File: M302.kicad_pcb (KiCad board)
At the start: 2 copper layers, 68.6 x 53.3 mm, 23 parts, among them J1 I2C-1, J2 I2C-2, J3 I2C-3, J4 I2C-4, J5 I2C-D400, J6 W5500, J7 IM920, J8 PWR, J9 VSW, P1 Power, P2 Analog, P3 Digital, P4 Digital, P5 CONN_01X01, P6 CONN_01X01, P7 CONN_01X01, P8 CONN_01X01, SW1 CPU_RESET, SW2 D400_RESET, SW3 IM920_RESET, U1 SFE-BOB-12009

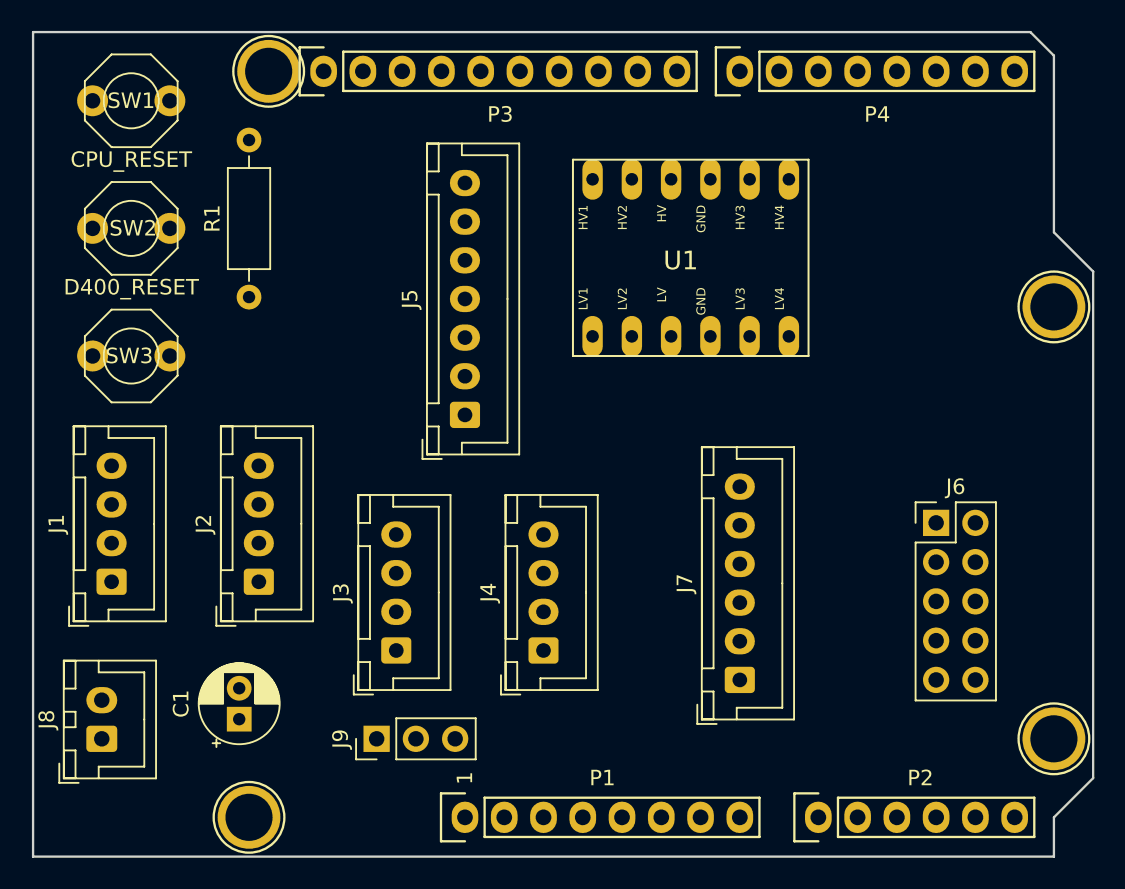
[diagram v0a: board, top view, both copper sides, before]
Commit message: VSWは不要なので外す
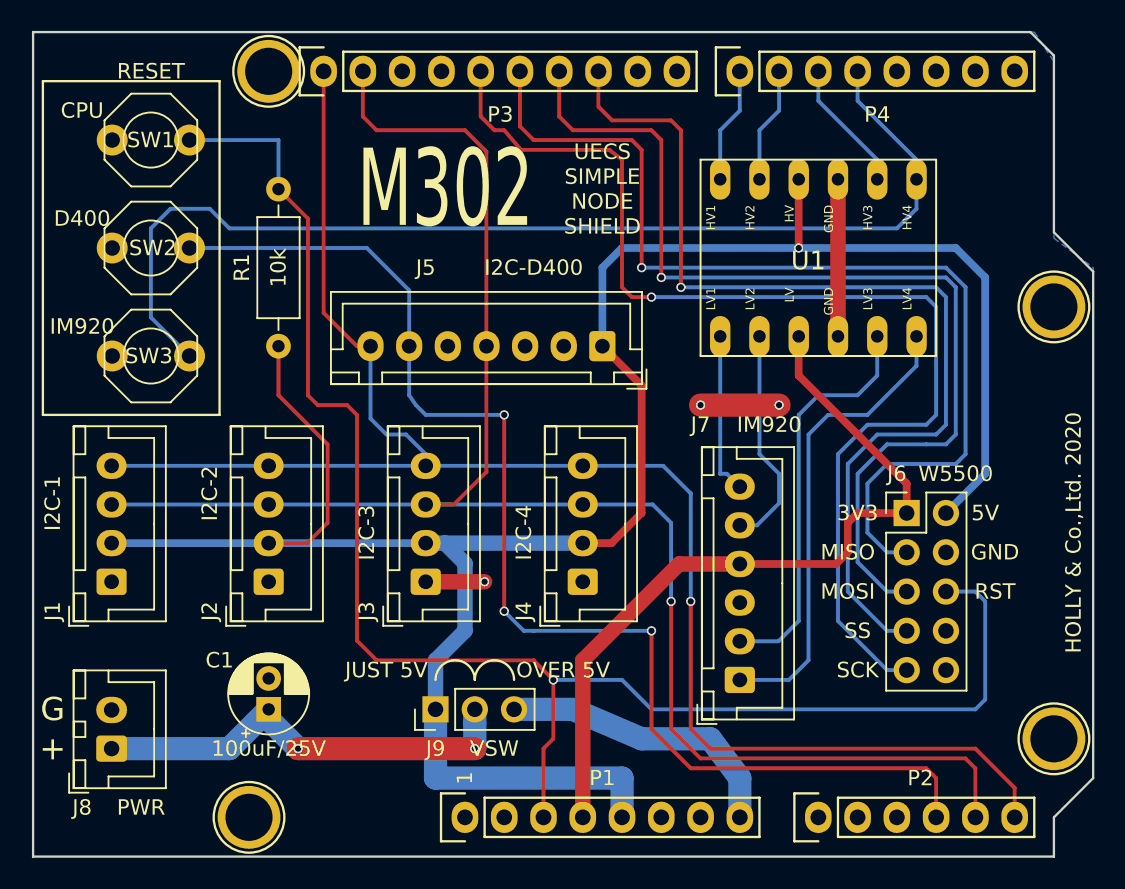
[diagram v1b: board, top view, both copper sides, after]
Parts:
- SW1: value CPU_RESET -> CPU
- SW2: value D400_RESET -> D400
- SW3: value IM920_RESET -> IM920
- moved J5 9.94 mm to (147.8, 93.3), turned to 180 degrees
- moved U1 8.25 mm to (161.8, 87.6)
- moved J4 5.12 mm to (146.6, 108.6)
- moved J3 4.84 mm to (136.4, 108.6)
- moved J9 4.26 mm to (137.0, 116.8)
- moved R1 3.70 mm to (126.9, 93.3)
- moved SW1 2.84 mm to (118.6, 80.0)
- moved J6 2.01 mm to (167.5, 104.1)
- moved C1 2.01 mm to (126.2, 116.8)
- moved SW2 1.80 mm to (118.6, 87.0)
- moved SW3 1.27 mm to (118.6, 94.0)
- moved J8 0.90 mm to (116.1, 119.4)
- moved J2 0.64 mm to (126.2, 108.6)
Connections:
- J6 pad 10: +5V -> Net-(J6-Pad10)
- J6 pad 2: /12(MISO) -> +5V
- J6 pad 3: /11(**/MOSI) -> /12(MISO)
- J6 pad 4: /10(**/SS) -> GND
- J6 pad 5: /13(SCK) -> /11(**/MOSI)
- J6 pad 6: Net-(J6-Pad6) -> /Reset
- J6 pad 7: Net-(J6-Pad7) -> /10(**/SS)
- J6 pad 8: /Reset -> Net-(J6-Pad8)
- J6 pad 9: GND -> /13(SCK)
- U1 pad HV1: /4 -> /7
- U1 pad HV2: /5(**) -> /6(**)
- U1 pad HV3: /6(**) -> /5(**)
- U1 pad HV4: /7 -> /4
- U1 pad LV1: Net-(J7-Pad1) -> Net-(J7-Pad6)
- U1 pad LV2: Net-(J7-Pad2) -> Net-(J7-Pad5)
- U1 pad LV3: Net-(J7-Pad5) -> Net-(J7-Pad2)
- U1 pad LV4: Net-(J7-Pad6) -> Net-(J7-Pad1)
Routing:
- net +5V: track 0.00 -> 148.3 mm, vias 0 -> 1
- net /A4(SDA): track 0.00 -> 111.3 mm, vias 0 -> 1
- net /A5(SCL): track 0.00 -> 107.4 mm, vias 0 -> 1
- net /Reset: track 0.00 -> 102.4 mm, vias 0 -> 1
- net /A3: track 0.00 -> 80.2 mm, vias 0 -> 3
- net /13(SCK): track 0.00 -> 73.3 mm, vias 0 -> 1
- net /4: track 0.00 -> 70.9 mm
- net /12(MISO): track 0.00 -> 65.3 mm, vias 0 -> 1
- net /11(**/MOSI): track 0.00 -> 65.0 mm, vias 0 -> 1
- net /10(**/SS): track 0.00 -> 64.6 mm, vias 0 -> 1
- net +3V3: track 0.00 -> 50.5 mm
- net Net-(J7-Pad1): track 0.00 -> 30.3 mm
- net Net-(C1-Pad1): track 0.00 -> 28.5 mm, vias 0 -> 2
- net Net-(J7-Pad2): track 0.00 -> 26.4 mm
- net /Vin: track 0.00 -> 18.8 mm
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- added copper zone on B.Cu, net GND
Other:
- board text added: "+"
- board text added: "3V3"
- board text added: "5V"
- board text added: "G"
- board text added: "GND"
- board text added: "HOLLY & Co.,Ltd. 2020"
- board text added: "JUST 5V"
- board text added: "M302"
- board text added: "MISO"
- board text added: "MOSI"
- board text added: "OVER 5V"
- board text added: "RESET"
- board text added: "RST"
- board text added: "SCK"
- board text added: "SCL"
- board text added: "SDA"
- board text added: "SS"
- board text added: "UECS SIMPLE NODE SHIELD"

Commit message: 現在基板確認中
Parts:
- removed J9: VSW, Connector_PinHeader_2.54mm:PinHeader_1x03_P2.54mm_Vertical
- J1: value I2C-1 -> I2C-SHT3x
- J2: value I2C-2 -> I2C-ThmCp
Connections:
- C1 pad 1: Net-(C1-Pad1) -> +5V
- J8 pad 1: Net-(C1-Pad1) -> +5V
- P1 pad 8: /Vin -> Net-(P1-Pad8)
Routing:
- net Net-(C1-Pad1): track 28.5 -> 0.00 mm, vias 2 -> 0
- net +5V: track 148.3 -> 171.7 mm
- net /Vin: track 18.8 -> 0.00 mm
- net /A3: track 80.2 -> 81.0 mm
- net GND: track 14.0 -> 14.6 mm
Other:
- board text removed: "JUST 5V"
- board text removed: "OVER 5V"
